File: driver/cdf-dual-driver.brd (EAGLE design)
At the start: 48.3 x 83.3 mm, 55 parts, among them IC1 R-789.0-0.5, IC2 7805TV, IC3 74AC14D, IC4 UCC27423, IC5 UCC27423, Q1 FDD8424H, Q2 FDD8424H, Q3 FDD8424H, Q4 FDD8424H

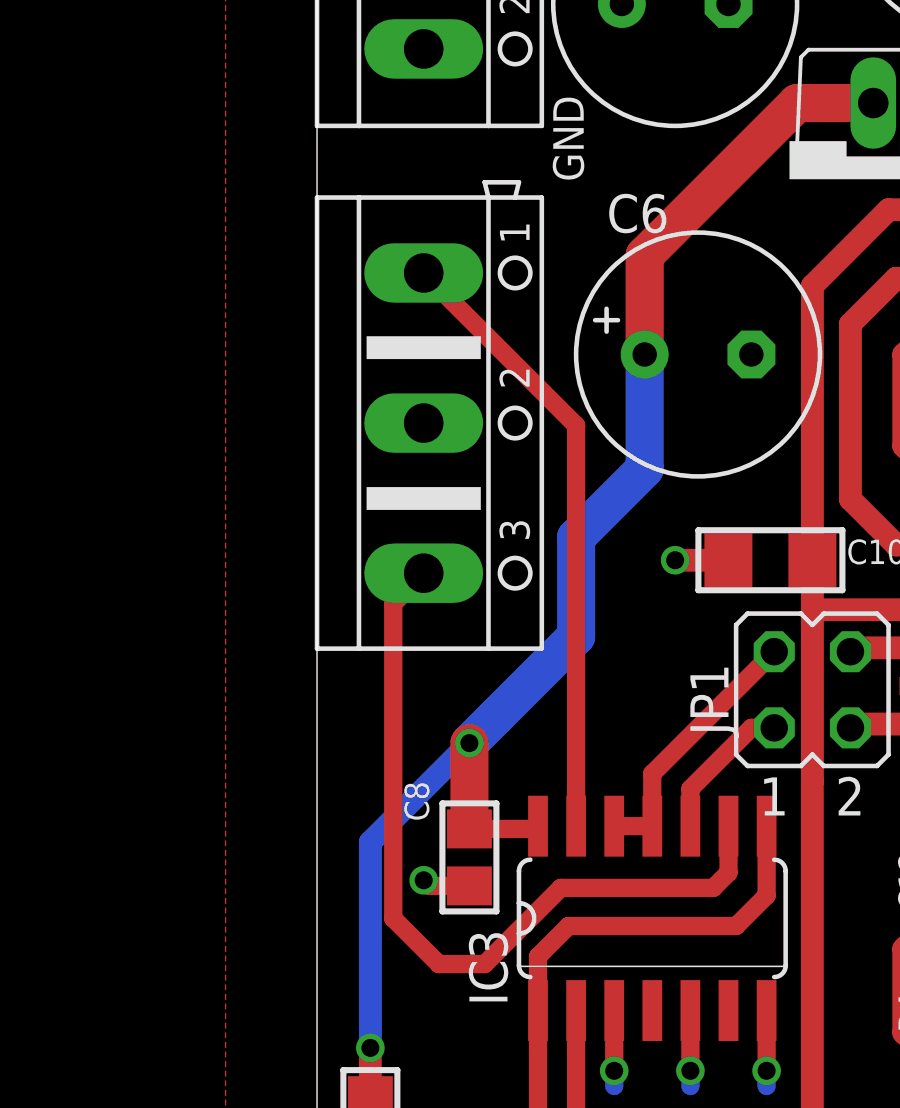
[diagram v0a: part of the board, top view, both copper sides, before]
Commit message: space connectors a bit more
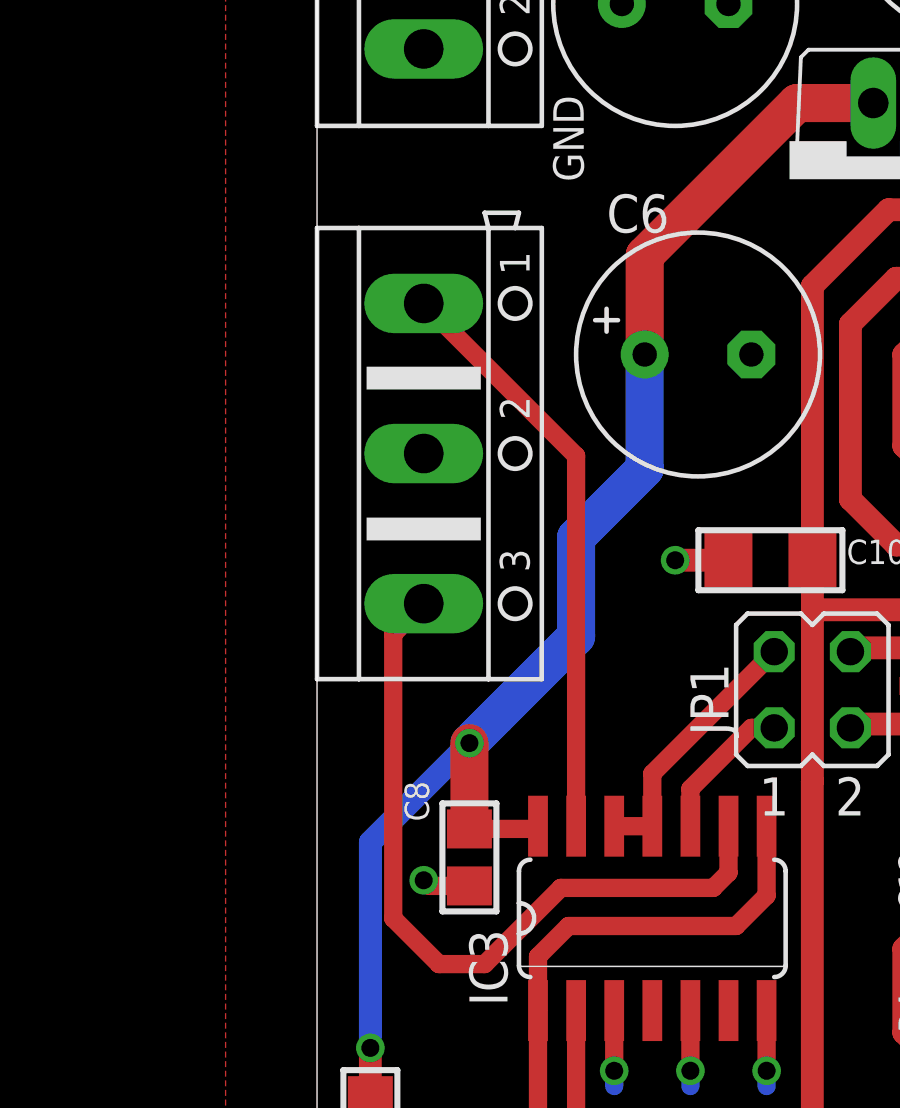
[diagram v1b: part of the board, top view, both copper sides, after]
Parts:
- moved GATE_IN 1.02 mm to (3.56, 55.1)
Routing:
- net N$25: track 26.5 -> 25.5 mm
- net N$24: track 20.5 -> 19.5 mm
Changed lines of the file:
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@@
 <attribute name="VALUE" x="19.939" y="12.954" size="1.27" layer="27" ratio="10" rot="R90"/>
 </element>
-<element name="GATE_IN" library="con-ptr500" package="AK500/3" value="" x="3.556" y="56.134" smashed="yes" rot="R270">
-<attribute name="MF" value="" x="3.556" y="56.134" size="1.778" layer="27" rot="R270" display="off"/>
-<attribute name="OC_FARNELL" value="unknown" x="3.556" y="56.134" size="1.778" layer="27" rot="R270" display="off"/>
-<attribute name="MPN" value="" x="3.556" y="56.134" size="1.778" layer="27" rot="R270" display="off"/>
-<attribute name="OC_NEWARK" value="unknown" x="3.556" y="56.134" size="1.778" layer="27" rot="R270" display="off"/>
-<attribute name="VALUE" x="-2.159" y="63.7286" size="1.778" layer="27" ratio="10" rot="R270"/>
+<element name="GATE_IN" library="con-ptr500" package="AK500/3" value="" x="3.556" y="55.118" smashed="yes" rot="R270">
+<attribute name="MF" value="" x="3.556" y="55.118" size="1.778" layer="27" rot="R270" display="off"/>
+<attribute name="OC_FARNELL" value="unknown" x="3.556" y="55.118" size="1.778" layer="27" rot="R270" display="off"/>
+<attribute name="MPN" value="" x="3.556" y="55.118" size="1.778" layer="27" rot="R270" display="off"/>
+<attribute name="OC_NEWARK" value="unknown" x="3.556" y="55.118" size="1.778" layer="27" rot="R270" display="off"/>
+<attribute name="VALUE" x="-2.159" y="62.7126" size="1.778" layer="27" ratio="10" rot="R270"/>
 </element>
 <element name="R2" library="microbuilder" package="0805" value="470" x="1.778" y="32.766" smashed="yes" rot="R270">
@@
 <contactref element="IC3" pad="13"/>
 <contactref element="GATE_IN" pad="1"/>
-<wire x1="8.636" y1="42.6974" x2="8.636" y2="56.0578" width="0.6096" layer="1"/>
-<wire x1="8.636" y1="56.0578" x2="3.556" y2="61.1378" width="0.6096" layer="1"/>
+<wire x1="8.636" y1="42.6974" x2="8.636" y2="55.0418" width="0.6096" layer="1"/>
+<wire x1="8.636" y1="55.0418" x2="3.556" y2="60.1218" width="0.6096" layer="1"/>
 </signal>
 <signal name="N$25">
@@
 <wire x1="5.588" y1="38.1" x2="4.064" y2="38.1" width="0.6096" layer="1"/>
 <wire x1="4.064" y1="38.1" x2="2.54" y2="39.624" width="0.6096" layer="1"/>
-<wire x1="2.54" y1="39.624" x2="2.54" y2="50.1142" width="0.6096" layer="1"/>
-<wire x1="2.54" y1="50.1142" x2="3.556" y2="51.1302" width="0.6096" layer="1"/>
+<wire x1="2.54" y1="39.624" x2="2.54" y2="49.0982" width="0.6096" layer="1"/>
+<wire x1="2.54" y1="49.0982" x2="3.556" y2="50.1142" width="0.6096" layer="1"/>
 </signal>
 </signals>
